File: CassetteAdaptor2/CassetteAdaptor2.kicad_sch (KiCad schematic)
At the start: 3 parts, among them J1 Cassette, J2 CS1 EAR, J3 CS1 MIC

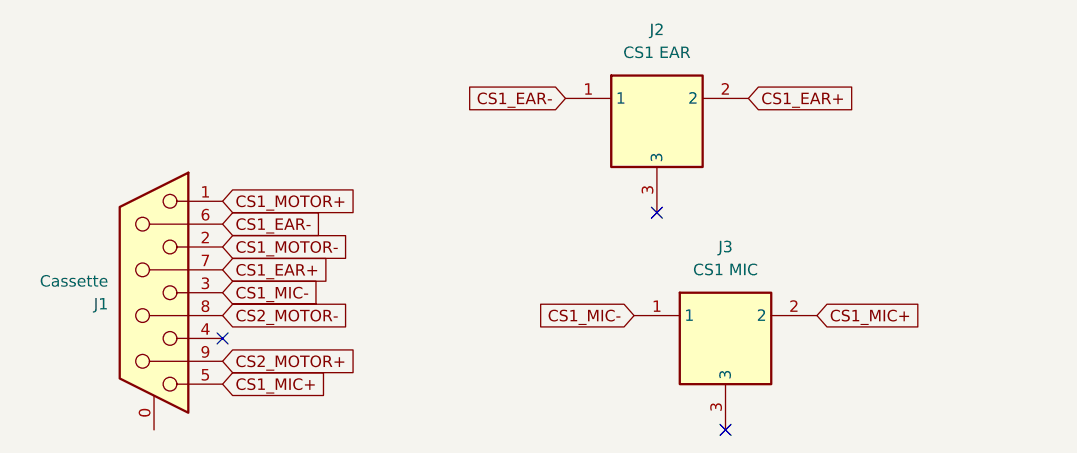
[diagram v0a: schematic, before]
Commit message: PCBs fabricated for testing
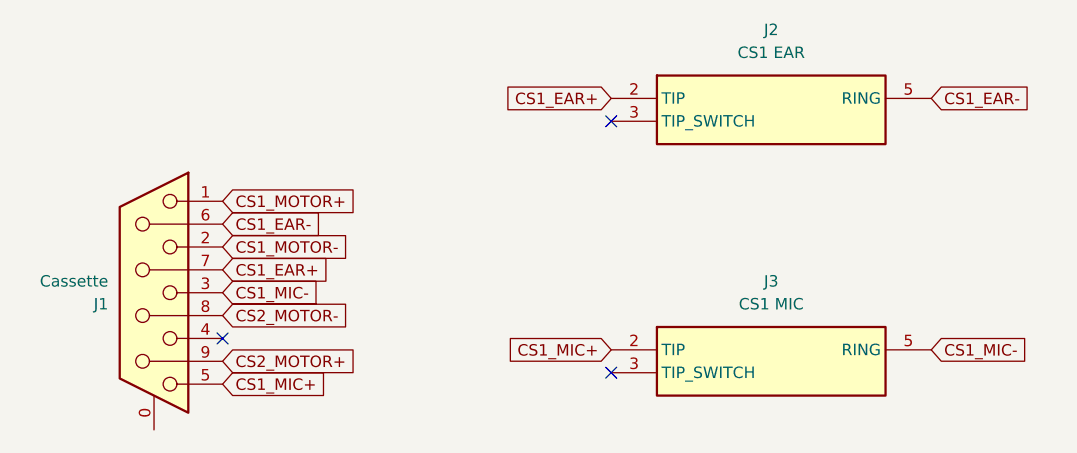
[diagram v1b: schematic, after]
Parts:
- removed J2: CS1 EAR, Clueless_Engineer:MJ3536N, symbol Clueless_Engineer:MJ-3536N_3.5mm_Mono_Socket
- removed J3: CS1 MIC, Clueless_Engineer:MJ3536N, symbol Clueless_Engineer:MJ-3536N_3.5mm_Mono_Socket
- added J2: CS1 EAR, Clueless_Engineer:SJ3350820BTR, symbol Clueless_Engineer:SJ3-350820B-TR
- added J3: CS1 MIC, Clueless_Engineer:SJ3350820BTR, symbol Clueless_Engineer:SJ3-350820B-TR
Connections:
- net CS1_EAR+: now also J2.2 (TIP)
- net CS1_EAR-: now also J2.5 (RING)
- net CS1_MIC+: now also J3.2 (TIP)
- net CS1_MIC-: now also J3.5 (RING)
